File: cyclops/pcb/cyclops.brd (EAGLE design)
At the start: 124.5 x 79.9 mm, 172 parts, among them Q4 IRF510, U1 MCP4921, U11 THS4281, U12 MAX4564, U13 ZXTD, U14 ZXTD, U15 OPA1664, U2 LT1931, U3 LT1764A, U4 BD60HC5WEFJ, U5 TPS72325, U6 LT1711, U7 TLV3701, U8 ADR03, U9 LT1880

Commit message: Minor layout.
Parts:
- moved TRIG 0.76 mm to (13.8, 0.00)
- moved VCTL 0.76 mm to (65.3, 79.9)
- moved VAUX_OUT 0.51 mm to (82.0, 79.9)
- moved VI 0.25 mm to (98.8, 79.9)
- moved VAUX_IN 0.25 mm to (30.9, 0.00)
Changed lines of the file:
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@@
 <text x="-6.35" y="11.811" size="1.016" layer="21" font="vector" ratio="18" align="center">SCL</text>
 <text x="-6.985" y="13.589" size="1.016" layer="21" font="vector" ratio="18" align="center">SDA</text>
-<text x="35.687" y="2.286" size="1.016" layer="21" font="vector" ratio="18" rot="R270" align="center">DGND</text>
-<text x="39.37" y="1.905" size="1.016" layer="21" font="vector" ratio="18" rot="R90" align="center">SCL</text>
-<text x="42.926" y="1.778" size="1.016" layer="21" font="vector" ratio="18" rot="R90" align="center">SDA</text>
+<text x="-12.065" y="11.938" size="1.016" layer="21" font="vector" ratio="18" rot="R270" align="center">DGND</text>
+<text x="-12.192" y="5.207" size="1.016" layer="21" font="vector" ratio="18" rot="R90" align="center">SCL</text>
+<text x="-11.176" y="7.874" size="1.016" layer="21" font="vector" ratio="18" rot="R90" align="center">SDA</text>
 <text x="2.667" y="6.858" size="1.016" layer="22" font="vector" ratio="18" rot="MR0" align="center">DGND</text>
 <text x="3.175" y="10.541" size="1.016" layer="22" font="vector" ratio="18" rot="MR0" align="center">SCL</text>
@@
 <attribute name="VALUE" x="86.36" y="24.384" size="1.016" layer="27" font="vector" ratio="18"/>
 </element>
-<element name="VAUX_OUT" library="jonnew" package="0731000105" value="0731000105" x="82.55" y="79.883" smashed="yes" rot="R180">
-<attribute name="NAME" x="84.0105" y="69.215" size="1.016" layer="25" font="vector" ratio="18"/>
-<attribute name="VALUE" x="87.249" y="79.629" size="1.016" layer="27" font="vector" ratio="18" rot="R180"/>
+<element name="VAUX_OUT" library="jonnew" package="0731000105" value="0731000105" x="82.042" y="79.883" smashed="yes" rot="R180">
+<attribute name="NAME" x="83.5025" y="69.215" size="1.016" layer="25" font="vector" ratio="18"/>
+<attribute name="VALUE" x="86.741" y="79.629" size="1.016" layer="27" font="vector" ratio="18" rot="R180"/>
 </element>
 <element name="REF2.1" library="cyclops" package="TP16R" value="TPTP16R" x="64.636" y="26.67" smashed="yes" rot="R90">
@@
 <attribute name="VALUE" x="11.811" y="57.39" size="1.016" layer="27" font="vector" ratio="18" rot="R180" align="center-left"/>
 </element>
-<element name="VI" library="jonnew" package="0731000105" value="0731000105" x="99.06" y="79.883" smashed="yes" rot="R180">
-<attribute name="NAME" x="100.711" y="69.215" size="1.016" layer="25" font="vector" ratio="18"/>
-<attribute name="VALUE" x="103.759" y="79.629" size="1.016" layer="27" font="vector" ratio="18" rot="R180"/>
+<element name="VI" library="jonnew" package="0731000105" value="0731000105" x="98.806" y="79.883" smashed="yes" rot="R180">
+<attribute name="NAME" x="100.457" y="69.215" size="1.016" layer="25" font="vector" ratio="18"/>
+<attribute name="VALUE" x="103.505" y="79.629" size="1.016" layer="27" font="vector" ratio="18" rot="R180"/>
 </element>
 <element name="VREF" library="jonnew" package="0731000105" value="0731000105" x="115.57" y="79.883" smashed="yes" rot="R180">
@@
 <attribute name="VALUE" x="120.269" y="79.629" size="1.016" layer="27" font="vector" ratio="18" rot="R180"/>
 </element>
-<element name="VCTL" library="jonnew" package="0731000105" value="0731000105" x="66.04" y="79.883" smashed="yes" rot="R180">
-<attribute name="NAME" x="67.564" y="69.215" size="1.016" layer="25" font="vector" ratio="18"/>
-<attribute name="VALUE" x="70.739" y="79.629" size="1.016" layer="27" font="vector" ratio="18" rot="R180"/>
+<element name="VCTL" library="jonnew" package="0731000105" value="0731000105" x="65.278" y="79.883" smashed="yes" rot="R180">
+<attribute name="NAME" x="66.802" y="69.215" size="1.016" layer="25" font="vector" ratio="18"/>
+<attribute name="VALUE" x="69.977" y="79.629" size="1.016" layer="27" font="vector" ratio="18" rot="R180"/>
 </element>
 <element name="PWR_DIST" library="cyclops" package="2X04-BIG" value="PINH2X4" x="115.796" y="56.954" smashed="yes" rot="R90">
@@
 <attribute name="VALUE" x="53.086" y="5.588" size="1.016" layer="27" font="vector" ratio="18" rot="R180"/>
 </element>
-<element name="VAUX_IN" library="jonnew" package="0731000105" value="0731000105" x="31.115" y="0" smashed="yes">
-<attribute name="NAME" x="32.512" y="9.652" size="1.016" layer="25" font="vector" ratio="18"/>
-<attribute name="VALUE" x="35.814" y="1.524" size="1.016" layer="27" font="vector" ratio="18" rot="R180"/>
+<element name="VAUX_IN" library="jonnew" package="0731000105" value="0731000105" x="30.861" y="0" smashed="yes">
+<attribute name="NAME" x="32.258" y="9.652" size="1.016" layer="25" font="vector" ratio="18"/>
+<attribute name="VALUE" x="35.56" y="1.524" size="1.016" layer="27" font="vector" ratio="18" rot="R180"/>
 </element>
 <element name="R38" library="cyclops" package="0603" value="2.2k" x="40.513" y="69.469" smashed="yes" rot="R270">
@@
 <attribute name="VALUE" x="42.799" y="-6.858" size="1.016" layer="27" font="vector" ratio="18" align="center-left"/>
 </element>
-<element name="TRIG" library="jonnew" package="0731000105" value="0731000105" x="14.605" y="0" smashed="yes">
-<attribute name="NAME" x="16.002" y="9.652" size="1.016" layer="25" font="vector" ratio="18"/>
-<attribute name="VALUE" x="19.304" y="1.27" size="1.016" layer="27" font="vector" ratio="18" rot="R180"/>
+<element name="TRIG" library="jonnew" package="0731000105" value="0731000105" x="13.843" y="0" smashed="yes">
+<attribute name="NAME" x="15.24" y="9.652" size="1.016" layer="25" font="vector" ratio="18"/>
+<attribute name="VALUE" x="18.542" y="1.27" size="1.016" layer="27" font="vector" ratio="18" rot="R180"/>
 </element>
 <element name="R30" library="cyclops" package="0603" value="1k" x="12.446" y="62.484" smashed="yes" rot="R270">
@@
 <via x="85.344" y="52.578" extent="1-16" drill="0.3302"/>
 <via x="85.344" y="51.308" extent="1-16" drill="0.3302"/>
-<via x="40.005" y="1.397" extent="1-16" drill="1.3" shape="octagon" alwaysstop="yes"/>
+<via x="45.085" y="-18.415" extent="1-16" drill="1.3" shape="octagon" alwaysstop="yes"/>
 <polygon width="0.1778" layer="1" thermals="no">
 <vertex x="98.806" y="63.5"/>
@@
 <wire x1="25.8064" y1="27.94" x2="25.8064" y2="25.4" width="0" layer="19" extent="1-1"/>
 <wire x1="-6.604" y1="8.255" x2="6.35" y2="1.524" width="0" layer="19" extent="1-1"/>
-<wire x1="54.737" y1="-26.416" x2="40.005" y2="1.397" width="0" layer="19" extent="1-1"/>
+<wire x1="54.737" y1="-26.416" x2="45.085" y2="-18.415" width="0" layer="19" extent="1-1"/>
 <wire x1="58.039" y1="-36.068" x2="54.737" y2="-26.416" width="0" layer="19" extent="1-1"/>
 <wire x1="-60.96" y1="-76.2" x2="-6.604" y2="8.255" width="0" layer="19" extent="1-1"/>
@@
 <contactref element="VCTL&lt;OFF&gt;DAC" pad="3"/>
 <wire x1="64.77" y1="79.121" x2="68.326" y2="75.565" width="0.3048" layer="1"/>
-<wire x1="66.04" y1="67.4878" x2="68.326" y2="75.565" width="0" layer="19" extent="1-1"/>
-<wire x1="17.3482" y1="64.77" x2="66.04" y2="67.4878" width="0" layer="19" extent="1-1"/>
+<wire x1="65.278" y1="67.4878" x2="68.326" y2="75.565" width="0" layer="19" extent="1-1"/>
+<wire x1="17.3482" y1="64.77" x2="65.278" y2="67.4878" width="0" layer="19" extent="1-1"/>
 </signal>
 <signal name="5V">
@@
 <wire x1="18.1864" y1="14.605" x2="18.1864" y2="16.51" width="0" layer="19" extent="1-1"/>
 <wire x1="18.1864" y1="12.7" x2="18.1864" y2="14.605" width="0" layer="19" extent="1-1"/>
-<wire x1="14.605" y1="12.3952" x2="18.1864" y2="12.7" width="0" layer="19" extent="1-1"/>
+<wire x1="13.843" y1="12.3952" x2="18.1864" y2="12.7" width="0" layer="19" extent="1-1"/>
 </signal>
 <signal name="T0">
@@
 <contactref element="VAUX_OUT" pad="1"/>
 <contactref element="R4" pad="1"/>
-<wire x1="-55.753" y1="-60.452" x2="82.55" y2="67.4878" width="0" layer="19" extent="1-1"/>
+<wire x1="-55.753" y1="-60.452" x2="82.042" y2="67.4878" width="0" layer="19" extent="1-1"/>
 </signal>
 <signal name="N$53">
 <contactref element="VAUX_IN" pad="1"/>
 <contactref element="R5" pad="1"/>
-<wire x1="31.115" y1="12.3952" x2="-55.753" y2="-72.644" width="0" layer="19" extent="1-1"/>
+<wire x1="30.861" y1="12.3952" x2="-55.753" y2="-72.644" width="0" layer="19" extent="1-1"/>
 </signal>
 <signal name="N$54">
 <contactref element="VI" pad="1"/>
 <contactref element="R6" pad="1"/>
-<wire x1="-55.753" y1="-66.548" x2="99.06" y2="67.4878" width="0" layer="19" extent="1-1"/>
+<wire x1="-55.753" y1="-66.548" x2="98.806" y2="67.4878" width="0" layer="19" extent="1-1"/>
 </signal>
 <signal name="N$55">

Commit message: More routing and notes.
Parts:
- removed R5: 50, jonnew:1206
- added C40: 10uF, jonnew:1206
- C15: device cyclops:1206 -> jonnew:0603
- moved R7 221.5 mm to (111.5, 68.3), turned to 180 degrees
- moved R6 201.0 mm to (94.7, 68.6), turned to 180 degrees
- moved R4 184.6 mm to (78.0, 68.6), turned to 180 degrees
- moved U4 181.6 mm to (59.4, 59.7), turned to 90 degrees
- moved U9 176.2 mm to (72.9, 29.2)
- moved C16 146.1 mm to (45.7, 52.3)
- moved C15 137.8 mm to (49.0, 49.3), turned to 90 degrees
- moved C13 136.5 mm to (42.4, 48.3), turned to 90 degrees
- moved U5 131.6 mm to (45.7, 49.3), turned to 270 degrees
- moved +6V 93.2 mm to (55.1, 57.1), turned to 180 degrees
- moved C12 91.2 mm to (59.4, 64.8), turned to 0 degrees
- moved C14 90.7 mm to (59.4, 54.6)
- moved J_ADDR4 54.9 mm to (-14.2, 56.9), turned to 180 degrees
- moved J_ADDR3 51.9 mm to (-14.2, 54.9), turned to 180 degrees
- moved J_ADDR2 49.2 mm to (-14.2, 52.8), turned to 180 degrees
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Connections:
- removed net N$48: C13.1, C16.1, U5.1
- removed net N$53: R5.1, VAUX_IN.1
- net +13.3V: now also C40.1; no longer C12.1, U4.5, U4.8
- net +15V: now also C12.1, U4.5, U4.8
- net +6V: now also C6.1, L3.3, U2.4, U2.5, U4.1
- net GND: now also C13.1, C16.1, C40.2, U4.4, U4.6, U4.7, U5.1
- net VAUX: now also VAUX_IN.1; no longer R5.2
- net VIN: no longer C6.1, L3.3, U2.4, U2.5
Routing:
- net LED+: track 63.5 -> 13.4 mm
- net LED-: track 79.2 -> 44.0 mm
- net VI: track 60.2 -> 32.9 mm
- net VAUX_OUT: track 45.2 -> 27.1 mm
- net REF5.0: track 57.2 -> 40.1 mm
- net +15V: track 42.4 -> 50.0 mm, vias 1 -> 3
- net -2.5V: track 43.0 -> 36.7 mm, vias 10 -> 9
- net REF2.5: track 43.7 -> 38.1 mm
- net OC: track 9.54 -> 3.95 mm
- net VINPUT: track 5.03 -> 0.00 mm
- net +6V: track 25.5 -> 29.7 mm, vias 9 -> 11
- net N$47: track 9.58 -> 5.77 mm
- net VREF: track 30.4 -> 27.7 mm
- net -5V: track 2.08 -> 0.00 mm, vias 1 -> 0
- net +3V3: track 2.08 -> 0.00 mm, vias 2 -> 0
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- added copper zone on layer 1, net +6V
- added copper zone on layer 15, net +6V
- added copper zone on layer 1, net -2.5V
- removed copper zone on layer 15, net +13.3V
- removed copper zone on layer 15, net VIN

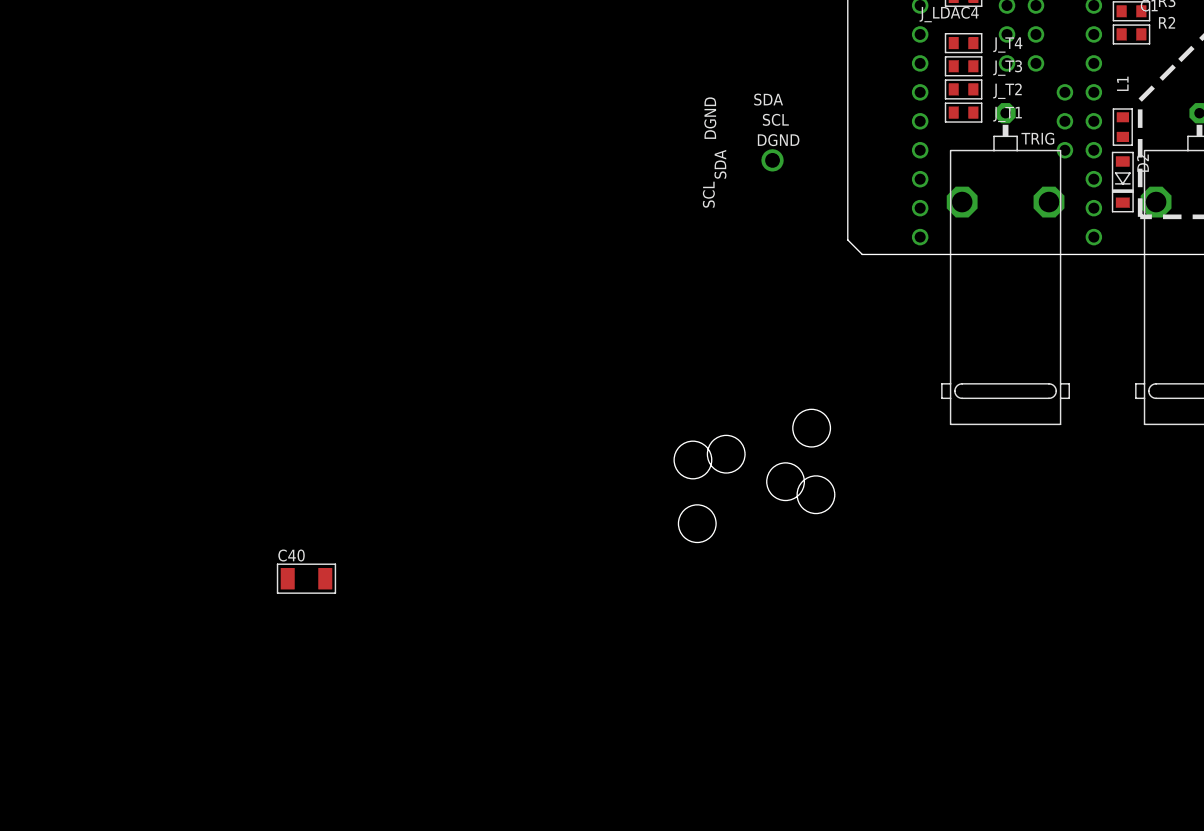
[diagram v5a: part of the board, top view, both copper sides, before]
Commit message: Started addining buck converter for digital rail.
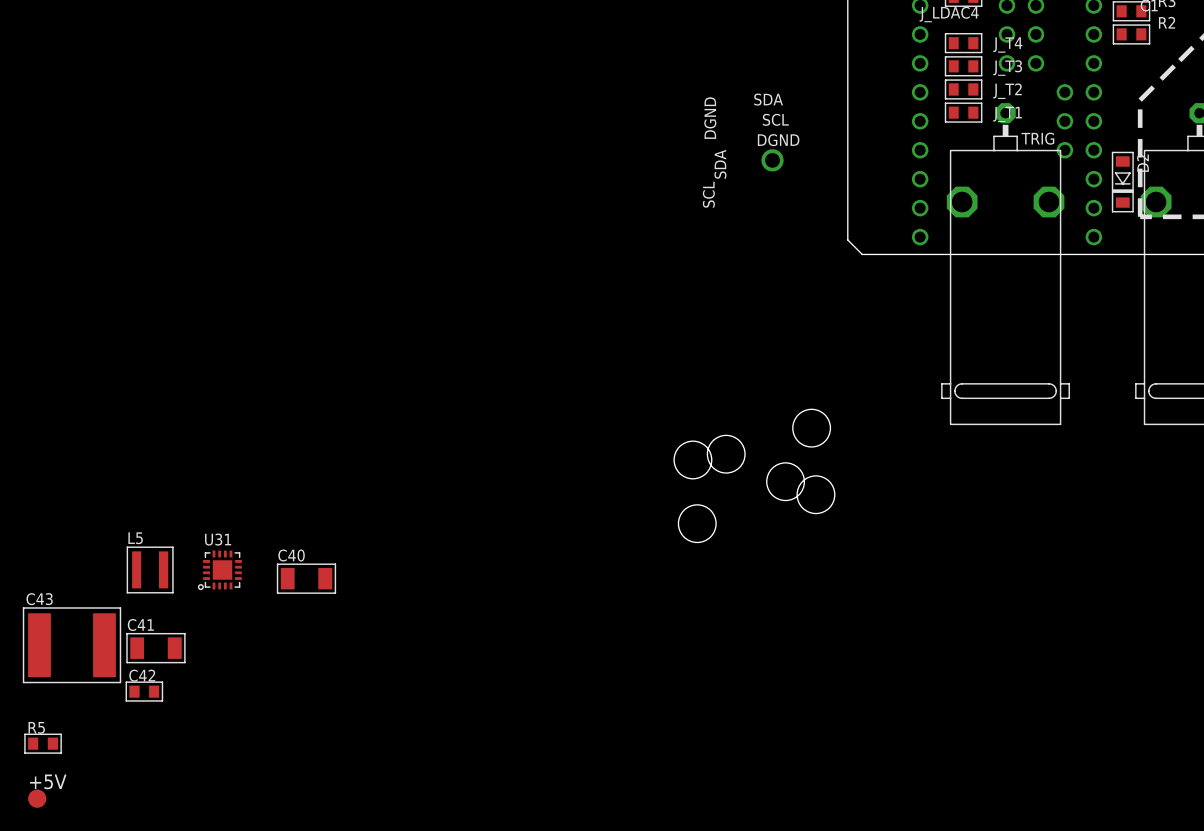
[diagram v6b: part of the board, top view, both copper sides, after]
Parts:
- removed L1: MPZ1608, cyclops:0603
- added +5V: TPTP16R, cyclops:TP16R
- added C41: 10uF, jonnew:1206
- added C42: 3.3nF, jonnew:0603
- added C43: 22uF, jonnew:2220
- added L5: XFL4020-222ME, jonnew:4020
- added R5: 100k, cyclops:0603
- added U31: TPS62153, jonnew:VQFN16
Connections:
- net VIN renamed TEENSY_VIN
- removed net N$43: D2.A, L1.1
- new net +5V: +5V.TP, C43.1, C6.1, D2.A, L3.3, L5.1, R5.2, U2.4, U2.5, U31.14
- new net N$48: U31.7, U31.8
- new net N$53: C41.2, C42.2
- new net N$56: C42.1, U31.9
- new net N$59: C43.2
- new net PG: R5.1, U31.4
- new net SW: L5.2, U31.1, U31.2, U31.3
- net +15V: now also C41.1, U31.10, U31.11, U31.12, U31.13
- net +6V: no longer C6.1, L1.2, L3.3, U2.4, U2.5
- net GND: now also U31.15, U31.16, U31.5, U31.6, U31.PAD
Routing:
- net +5V: track 0.00 -> 1.68 mm
- net +6V: track 29.7 -> 28.0 mm
